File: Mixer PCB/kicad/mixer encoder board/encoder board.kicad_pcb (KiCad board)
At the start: 2 copper layers, 161 x 28.5 mm, 17 parts, among them J1 Conn_02x13_Odd_Even, U10 PEC11R-4015F-S0024, U11 PEC11R-4015F-S0024, U12 PEC11R-4015F-S0024, U5 PEC11R-4015F-S0024, U6 PEC11R-4015F-S0024, U7 PEC11R-4015F-S0024, U8 PEC11R-4015F-S0024, U9 PEC11R-4015F-S0024

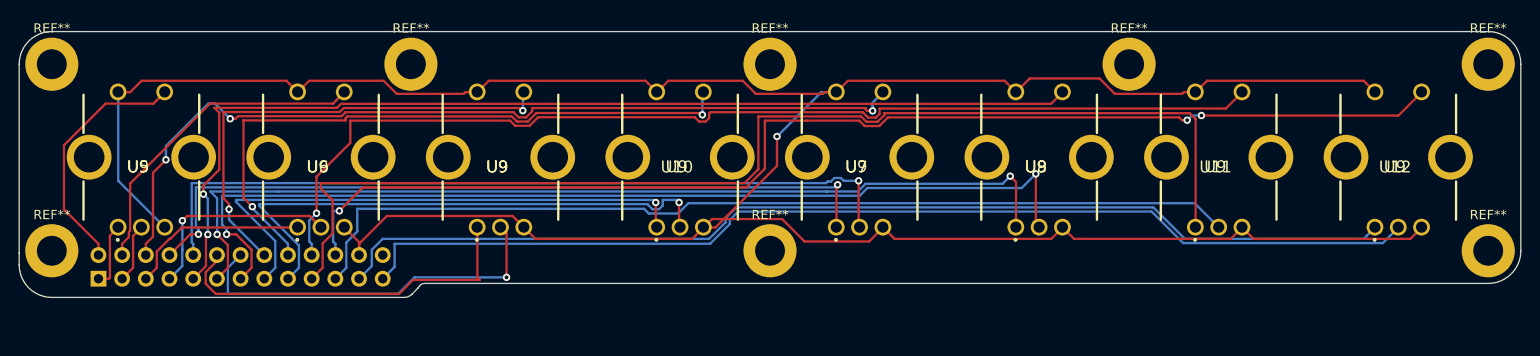
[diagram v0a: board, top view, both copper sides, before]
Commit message: add I2C motor driver board
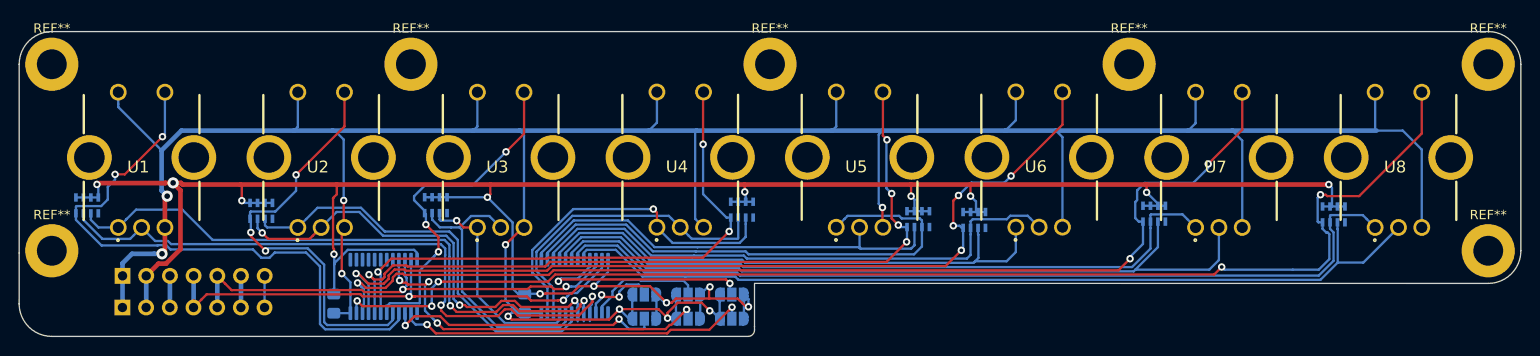
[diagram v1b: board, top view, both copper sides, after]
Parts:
- removed the REF** at (77.0, 50.0)
- removed U10, U11, U12, U9: PEC11R-4015F-S0024, custom:pec
- added C1: C, Capacitor_SMD:C_0805_2012Metric_Pad1.15x1.40mm_HandSolder, B.Cu at (30.2, 55.7)
- added C2: C, Capacitor_SMD:C_0805_2012Metric_Pad1.15x1.40mm_HandSolder, B.Cu at (50.7, 55.7)
- added J2: Conn_01x07, Connector_PinSocket_2.54mm:PinSocket_1x07_P2.54mm_Vertical, B.Cu at (7.57, 56.1)
- added JP1: SolderJumper_3_Open, Jumper:SolderJumper-3_P1.3mm_Open_RoundedPad1.0x1.5mm_NumberLabels, B.Cu at (72.9, 54.7)
- added JP2: SolderJumper_3_Open, Jumper:SolderJumper-3_P1.3mm_Open_RoundedPad1.0x1.5mm_NumberLabels, B.Cu at (68.2, 54.7)
- added JP3: SolderJumper_3_Open, Jumper:SolderJumper-3_P1.3mm_Open_RoundedPad1.0x1.5mm_NumberLabels, B.Cu at (63.5, 54.7)
- added JP4: SolderJumper_3_Open, Jumper:SolderJumper-3_P1.3mm_Open_RoundedPad1.0x1.5mm_NumberLabels, B.Cu at (68.2, 57.3)
- added JP5: SolderJumper_3_Open, Jumper:SolderJumper-3_P1.3mm_Open_RoundedPad1.0x1.5mm_NumberLabels, B.Cu at (72.9, 57.3)
- added JP6: SolderJumper_3_Open, Jumper:SolderJumper-3_P1.3mm_Open_RoundedPad1.0x1.5mm_NumberLabels, B.Cu at (63.5, 57.3)
- added RN1: R_Pack04, Resistor_SMD:R_Array_Concave_4x0603, B.Cu at (3.78, 45.1)
- added RN2: R_Pack04, Resistor_SMD:R_Array_Concave_4x0603, B.Cu at (22.5, 45.7)
- added RN3: R_Pack04, Resistor_SMD:R_Array_Concave_4x0603, B.Cu at (41.2, 45.1)
- added RN4: R_Pack04, Resistor_SMD:R_Array_Concave_4x0603, B.Cu at (74.0, 45.6)
- added RN5: R_Pack04, Resistor_SMD:R_Array_Concave_4x0603, B.Cu at (92.9, 46.6)
- added RN6: R_Pack04, Resistor_SMD:R_Array_Concave_4x0603, B.Cu at (98.9, 46.7)
- added RN7: R_Pack04, Resistor_SMD:R_Array_Concave_4x0603, B.Cu at (118.2, 46.0)
- added RN8: R_Pack04, Resistor_SMD:R_Array_Concave_4x0603, B.Cu at (137.4, 46.1)
- added U1: PEC11R-4015F-S0024, SamacSys_Parts:PEC12R-4XXXF-SXXXX_1, F.Cu at (9.62, 40.0)
- added U2: PEC11R-4015F-S0024, SamacSys_Parts:PEC12R-4XXXF-SXXXX_1, F.Cu at (28.9, 40.0)
- added U3: PEC11R-4015F-S0024, SamacSys_Parts:PEC12R-4XXXF-SXXXX_1, F.Cu at (48.1, 40.0)
- added U4: PEC11R-4015F-S0024, SamacSys_Parts:PEC12R-4XXXF-SXXXX_1, F.Cu at (67.4, 40.0)
- added ic1: PCA9555, Package_SO:TSSOP-24_4.4x7.8mm_P0.65mm, B.Cu at (35.6, 53.8)
- added ic2: PCA9555, Package_SO:TSSOP-24_4.4x7.8mm_P0.65mm, B.Cu at (56.1, 53.8)
- J1: value Conn_02x13_Odd_Even -> Conn_01x07; footprint Connector_PinSocket_2.54mm:PinSocket_2x13_P2.54mm_Vertical -> Connector_PinSocket_2.54mm:PinSocket_1x07_P2.54mm_Vertical
- U5, U6, U7, U8: footprint custom:pec -> SamacSys_Parts:PEC12R-4XXXF-SXXXX_1
- moved U6 77.0 mm to (105.9, 40.0)
- moved U5 77.0 mm to (86.6, 40.0)
- moved U7 38.5 mm to (125.1, 40.0)
- moved U8 38.5 mm to (144.4, 40.0)
- moved J1 2.60 mm to (7.58, 52.7)
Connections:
- J1 pad 1: Encoder1A -> GND
- J1 pad 2: Encoder1Button -> +3V3
- J1 pad 3: Encoder1B -> +5V
- J1 pad 4: Encoder2Button -> SDA
- J1 pad 5: Encoder2A -> SCL
- J1 pad 6: Encoder3Button -> LEDIN
- J1 pad 7: Encoder2B -> LEDOUT1
- U5 pad 1: Encoder1A -> Encoder5A
- U5 pad 3: Encoder1B -> Encoder5B
- U5 pad 5: Encoder1Button -> Encoder5Button
- U6 pad 1: Encoder2A -> Encoder6A
- U6 pad 3: Encoder2B -> Encoder6B
- U6 pad 5: Encoder2Button -> Encoder6Button
- U7 pad 1: Encoder3A -> Encoder7A
- U7 pad 3: Encoder3B -> Encoder7B
- U7 pad 5: Encoder3Button -> Encoder7Button
- U8 pad 1: Encoder4A -> Encoder8A
- U8 pad 3: Encoder4B -> Encoder8B
- U8 pad 5: Encoder4Button -> Encoder8Button
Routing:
- net +3V3: track 0.00 -> 268.1 mm, vias 0 -> 15
- net Encoder4B: track 105.4 -> 33.8 mm, vias 2 -> 0
- net Encoder4A: track 102.9 -> 36.9 mm, vias 2 -> 1
- net Encoder1B: track 6.36 -> 69.6 mm, vias 0 -> 2
- net Encoder3A: track 82.9 -> 23.3 mm, vias 2 -> 1
- net Encoder1A: track 7.02 -> 66.5 mm, vias 0 -> 2
- net Encoder3Button: track 94.8 -> 36.9 mm
- net SDA: track 0.00 -> 55.1 mm, vias 0 -> 2
- net Encoder3B: track 84.7 -> 30.2 mm, vias 1 -> 0
- net Encoder4Button: track 111.7 -> 60.5 mm, vias 2 -> 3
- net SCL: track 0.00 -> 50.4 mm, vias 0 -> 2
- net Encoder7A: track 124.4 -> 75.3 mm
- net A0_I2C1: track 0.00 -> 39.8 mm, vias 0 -> 4
- net A1_I2C1: track 0.00 -> 38.2 mm, vias 0 -> 2
- net Encoder1Button: track 26.5 -> 64.5 mm, vias 0 -> 2
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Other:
- board size 161 x 28.5 mm -> 161 x 32.7 mm
